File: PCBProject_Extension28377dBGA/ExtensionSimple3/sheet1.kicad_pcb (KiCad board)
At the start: 4 copper layers, 140.3 x 101.7 mm, 112 parts, among them J1 Conn_02x05_Odd_Even, J2 Conn_01x02_Pin, J3 Conn_01x02_Pin, J4 Conn_01x02_Pin, J5 Conn_01x02_Pin, Q1 FMMT618TA, U1 SN74ABT541, U2 SN74ABT541

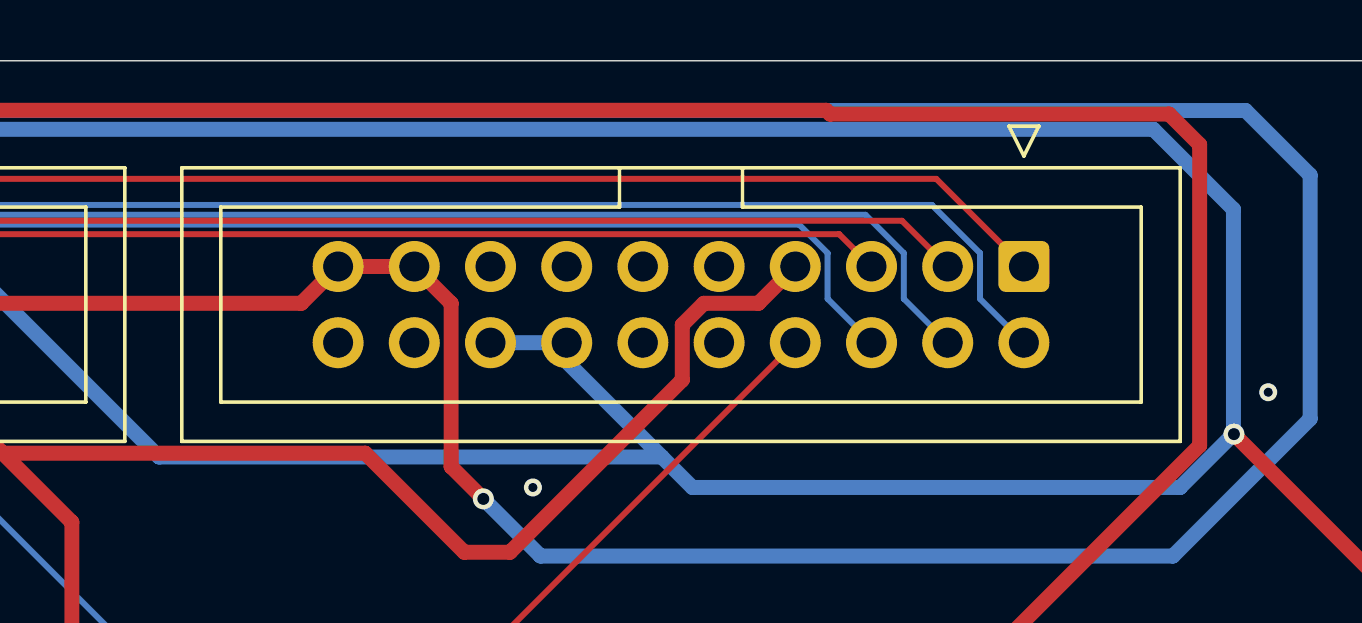
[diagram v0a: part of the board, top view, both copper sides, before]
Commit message: @Eorl 1. 需要第二套高速SPI，把 SPI-A 引出来用于DSP之间50MHz通讯。 2. 给I2C找到合适的GPIO引脚，更新原理图 3. 随便找一排GPIO引脚拉到2.54mm的排针上，为INPUT-XBAR预留 4. CAN的12V电源应该是数字电源，现在是用电流传感器的12V，not good 5. CAN排针之间太近，485排针之间太近 6. QEP不需要那个2*10的简牛，删了 7. D12V按原则走外围，不要走DSP下面。
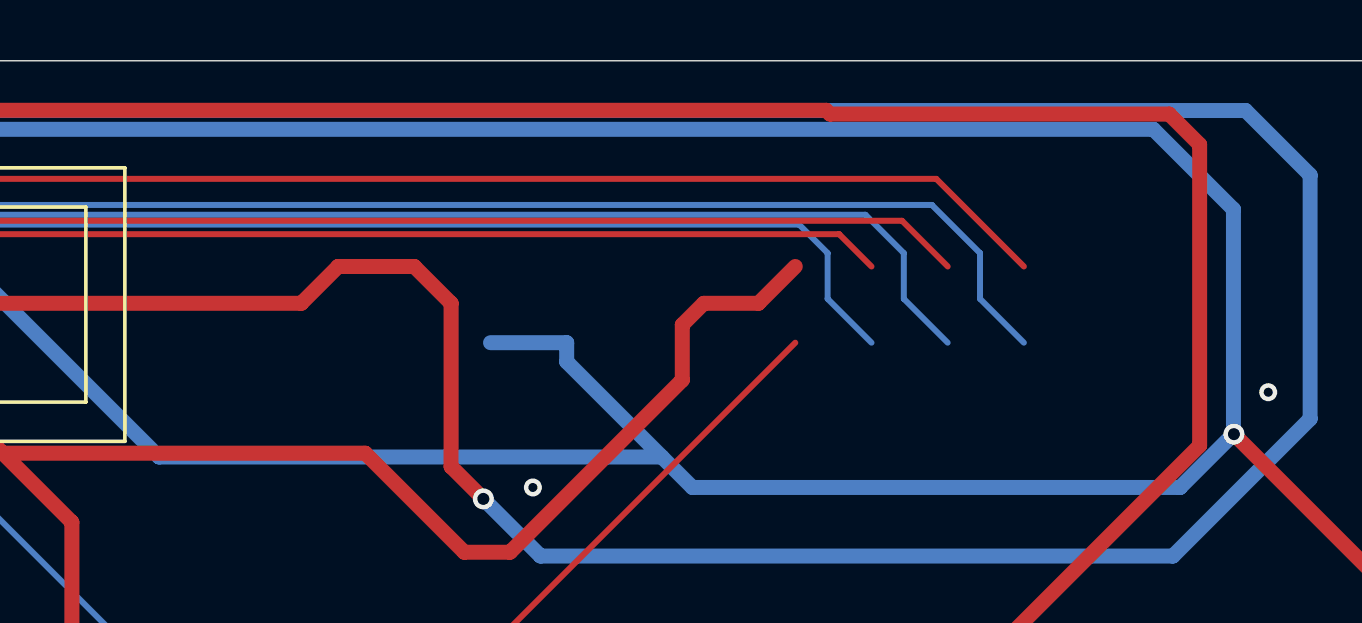
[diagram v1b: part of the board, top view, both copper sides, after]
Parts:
- removed INC1: HIF3FC-20PA-2.54DSA, Connector_IDC:IDC-Header_2x10_P2.54mm_Vertical

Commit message: finish 7 commits
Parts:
- added BiSS_C1: Conn_01x05, Connector_PinHeader_2.54mm:PinHeader_1x05_P2.54mm_Vertical, F.Cu at (271.3, 70.0)
- added J6: Conn_02x05_Odd_Even, Connector_PinHeader_2.54mm:PinHeader_2x05_P2.54mm_Vertical, B.Cu at (316.6, 149.4)
- added SPI3: Conn_02x04_Counter_Clockwise, Connector_PinSocket_2.54mm:PinSocket_2x04_P2.54mm_Vertical, F.Cu at (260.5, 71.0)
- moved UART1 18.0 mm to (270.0, 158.4)
- moved Q1 17.5 mm to (196.0, 81.3)
- moved R30 17.2 mm to (199.4, 81.4)
- moved R31 15.3 mm to (197.2, 78.2), turned to 0 degrees
- moved R29 13.0 mm to (202.3, 80.2)
- moved D3 12.3 mm to (202.3, 78.1), turned to 180 degrees
- moved UART2 10.1 mm to (257.4, 158.4)
- moved CAN_A1 6.77 mm to (210.6, 79.7)
- moved UART4 6.01 mm to (232.1, 158.4)
- moved CAN_B1 2.64 mm to (210.6, 66.1)
- moved UART3 2.50 mm to (244.8, 158.4)
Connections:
- CAN_A1 pad 1: +12 -> D12V1
- CAN_B1 pad 1: +12 -> D12V1
- DSP1 pad 124: unconnected-(DSP1-CS2_124-Pad124) -> /TX_DIR
- DSP1 pad 149: unconnected-(DSP1-149_GP1-Pad149) -> /MSCLA
- DSP1 pad 150: unconnected-(DSP1-GP0_150-Pad150) -> /MSDAA
- DSP1 pad 25: /MQEP2A -> /DATA_IN
- DSP1 pad 26: /MQEP2B -> /DATA_OUT
- DSP1 pad 27: /MQEP2S -> /SPICLK
- DSP1 pad 28: /MQEP2Z -> AGND
- DSP1 pad 38: unconnected-(DSP1-GP7_38-Pad38) -> /SPICLK
- DSP1 pad 66: /QEP2_HALL_V -> /PWR_CTL
- RU1 pad 1: REF_3V -> unconnected-(RU1-Pad1)
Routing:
- net PE_GND: track 312.1 -> 176.0 mm
- net D12V1: track 231.4 -> 344.8 mm, vias 4 -> 2
- net VDD: track 371.7 -> 267.5 mm
- net /TX_DIR: track 0.00 -> 89.3 mm
- net /MSDAA: track 0.00 -> 79.2 mm
- net /MSCLA: track 0.00 -> 73.3 mm, vias 0 -> 1
- net REF_3V: track 82.7 -> 154.1 mm, vias 0 -> 2
- net /DATA_OUT: track 0.00 -> 56.1 mm
- net /SPICLK: track 0.00 -> 49.8 mm, vias 0 -> 1
- net /QEP1_HALL_U: track 86.0 -> 36.3 mm
- net /MQEP1A: track 70.4 -> 21.4 mm
- net /DATA_IN: track 0.00 -> 46.6 mm, vias 0 -> 1
- net /MQEP1S: track 43.9 -> 0.00 mm, vias 1 -> 0
- net /MQEP1B: track 67.9 -> 24.3 mm
- net /QEP1_HALL_V: track 75.0 -> 31.5 mm
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
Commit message: finish happy485
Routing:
- net AGND: vias 111 -> 112
